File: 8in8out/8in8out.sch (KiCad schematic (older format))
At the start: 122 parts, among them IC1 ATTINY2313-P, J1 RJ45, J2 RJ45, J3 CONN_6, K110 G5T-1-12VDC, K120 G5T-1-12VDC, K130 G5T-1-12VDC, K140 G5T-1-12VDC, K150 G5T-1-12VDC, K160 G5T-1-12VDC, K170 G5T-1-12VDC, K180 G5T-1-12VDC, P1 CONN_5, P100 CONN_2, P101 CONN_2, P102 CONN_2, P103 CONN_2, P105 CONN_2, P106 CONN_2, P107 CONN_3, P109 CONN_2, P110 CONN_2, P120 CONN_2, P130 CONN_2, P140 CONN_2, P150 CONN_2, P160 CONN_2, P170 CONN_2, P180 CONN_2, P2 CONN_5, Q110 NPN, Q120 NPN, Q130 NPN, Q140 NPN, Q150 NPN, Q160 NPN, Q170 NPN, Q180 NPN, U1 74HC595, U10 OPTO-TRANSISTOR, U2 74LS165, U20 OPTO-TRANSISTOR, U30 OPTO-TRANSISTOR, U40 OPTO-TRANSISTOR, U50 OPTO-TRANSISTOR, U60 OPTO-TRANSISTOR, U70 OPTO-TRANSISTOR, U80 OPTO-TRANSISTOR

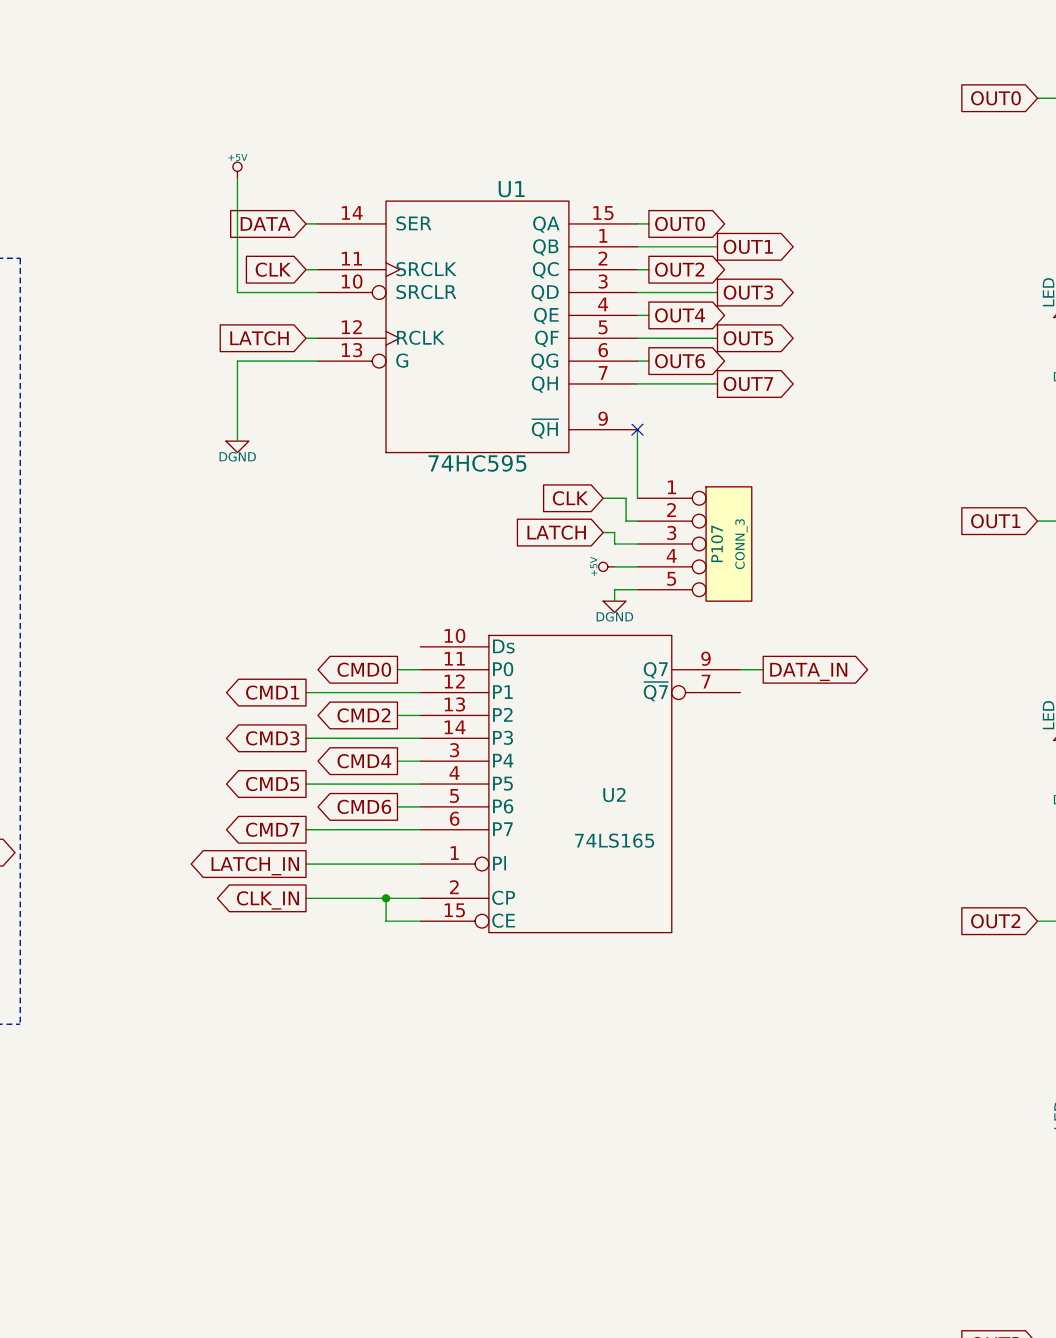
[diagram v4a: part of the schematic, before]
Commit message: Modification 74HC165
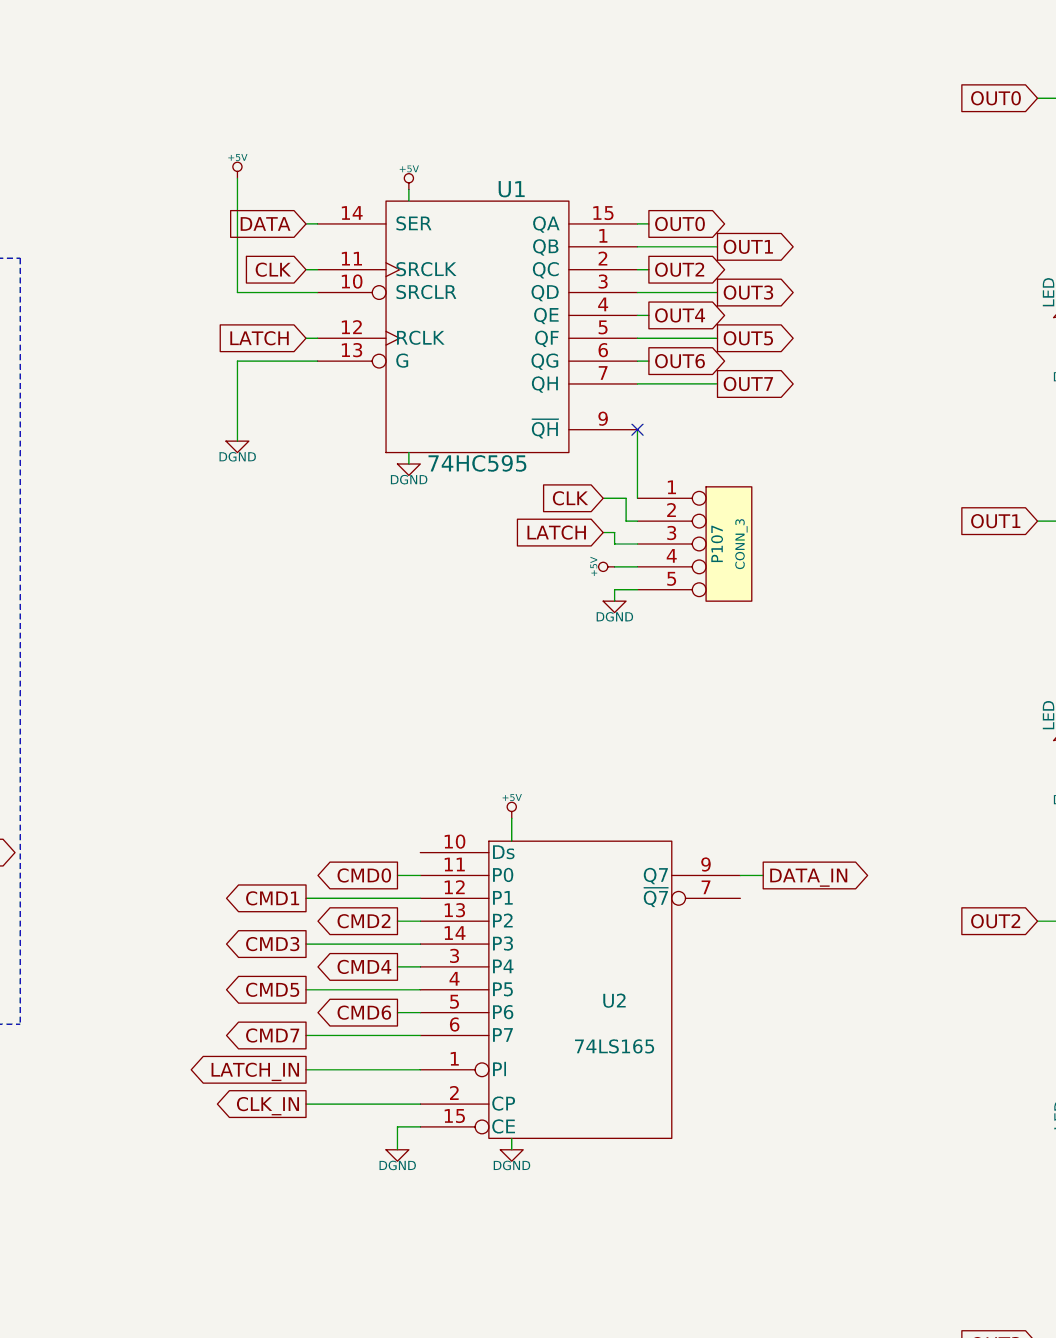
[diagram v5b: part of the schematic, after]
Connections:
- net GND is gone; now on net DGND: P1.5, P2.5, R10.2, R11.2, R20.2, R21.2, R30.2, R31.2, R40.2, R41.2, R50.2, R51.2, R60.2, R61.2, R70.2, R71.2, R80.2, R81.2, U1.8 (GND), U2.8 (GND)
- net CLK_IN: no longer U2.15 (CE)
- net DGND: now also U2.15 (CE)
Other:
- moved on the sheet: U2
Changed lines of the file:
@@
-EESchema Schematic File Version 2  date dim. 10 févr. 2013 15:59:09 CET
+EESchema Schematic File Version 2  date dim. 10 févr. 2013 20:44:48 CET
 LIBS:g5la-1-12vdc
 LIBS:power
@@
 Text GLabel 3950 13200 2    60   Input ~ 0
 CMD7
-Text GLabel 11200 8000 0    60   Output ~ 0
+Text GLabel 11200 8900 0    60   Output ~ 0
 CMD2
-Text GLabel 11200 7800 0    60   Output ~ 0
+Text GLabel 11200 8700 0    60   Output ~ 0
 CMD0
-Text GLabel 10800 8100 0    60   Output ~ 0
+Text GLabel 10800 9000 0    60   Output ~ 0
 CMD3
-Text GLabel 10800 7900 0    60   Output ~ 0
+Text GLabel 10800 8800 0    60   Output ~ 0
 CMD1
-Text GLabel 11200 8200 0    60   Output ~ 0
+Text GLabel 11200 9100 0    60   Output ~ 0
 CMD4
 Text GLabel 8850 7800 2    60   Output ~ 0
@@
 Wire Notes Line
 	5550 5800 5550 3500
-Text GLabel 10800 8500 0    60   Output ~ 0
+Text GLabel 10800 9400 0    60   Output ~ 0
 CMD7
-Text GLabel 11200 8400 0    60   Output ~ 0
+Text GLabel 11200 9300 0    60   Output ~ 0
 CMD6
-Text GLabel 10800 8300 0    60   Output ~ 0
+Text GLabel 10800 9200 0    60   Output ~ 0
 CMD5
 Wire Notes Line
@@
 L 74LS165 U2
 U 1 1 5116CE96
-P 12000 8300
-F 0 "U2" H 12150 8250 60  0000 C CNN
-F 1 "74LS165" H 12150 8050 60  0000 C CNN
-	1    12000 8300
+P 12000 9200
+F 0 "U2" H 12150 9150 60  0000 C CNN
+F 1 "74LS165" H 12150 8950 60  0000 C CNN
+	1    12000 9200
 	1    0    0    -1
 $EndComp
 Wire Wire Line
-	10800 7900 11300 7900
+	10800 8800 11300 8800
 Wire Wire Line
-	11300 8000 11200 8000
+	11300 8900 11200 8900
 Wire Wire Line
-	10800 8100 11300 8100
+	10800 9000 11300 9000
 Wire Wire Line
-	11300 8200 11200 8200
+	11300 9100 11200 9100
 Wire Wire Line
-	10800 8300 11300 8300
+	10800 9200 11300 9200
 Wire Wire Line
-	11300 8400 11200 8400
+	11300 9300 11200 9300
 Wire Wire Line
-	10800 8500 11300 8500
-Text GLabel 10800 8650 0    60   Output ~ 0
+	10800 9400 11300 9400
+Text GLabel 10800 9550 0    60   Output ~ 0
 LATCH_IN
-Text GLabel 10800 8800 0    60   Output ~ 0
+Text GLabel 10800 9700 0    60   Output ~ 0
 CLK_IN
 Wire Wire Line
-	11300 8650 10800 8650
+	11300 9550 10800 9550
 Text GLabel 9050 3100 3    60   Output ~ 0
 A0
@@
 	8350 8200 8400 8200
 Wire Wire Line
-	10800 8800 11300 8800
-Wire Wire Line
-	11150 8900 11300 8900
-Text GLabel 12800 7800 2    60   Output ~ 0
+	10800 9700 11300 9700
+Text GLabel 12800 8700 2    60   Output ~ 0
 DATA_IN
 Wire Wire Line
-	11150 8900 11150 8800
-Connection ~ 11150 8800
-Wire Wire Line
 	5950 7600 6050 7600
 Wire Wire Line
@@
 DATA_IN
 Wire Wire Line
-	11300 7800 11200 7800
+	11300 8700 11200 8700
 NoConn ~ 12250 6750
 Wire Wire Line
@@
 $EndComp
 $Comp
-L +5V #PWR093
+L +5V #PWR091
 U 1 1 51172614
 P 3800 2550
-F 0 "#PWR093" H 3800 2640 20  0001 C CNN
+F 0 "#PWR091" H 3800 2640 20  0001 C CNN
 F 1 "+5V" H 3800 2640 30  0000 C CNN
 	1    3800 2550
@@
 $EndComp
 $Comp
-L +5V #PWR094
+L +5V #PWR092
 U 1 1 51172694
 P 3800 4000
-F 0 "#PWR094" H 3800 4090 20  0001 C CNN
+F 0 "#PWR092" H 3800 4090 20  0001 C CNN
 F 1 "+5V" H 3800 4090 30  0000 C CNN
 	1    3800 4000
@@
 $EndComp
 $Comp
-L +5V #PWR095
+L +5V #PWR093
 U 1 1 511726A0
 P 3800 5450
-F 0 "#PWR095" H 3800 5540 20  0001 C CNN
+F 0 "#PWR093" H 3800 5540 20  0001 C CNN
 F 1 "+5V" H 3800 5540 30  0000 C CNN
 	1    3800 5450
@@
 $EndComp
 $Comp
-L +5V #PWR096
+L +5V #PWR094
 U 1 1 511726AC
 P 3800 6900
-F 0 "#PWR096" H 3800 6990 20  0001 C CNN
+F 0 "#PWR094" H 3800 6990 20  0001 C CNN
 F 1 "+5V" H 3800 6990 30  0000 C CNN
 	1    3800 6900
@@
 $EndComp
 $Comp
-L +5V #PWR097
+L +5V #PWR095
 U 1 1 511726B8
 P 3800 8350
-F 0 "#PWR097" H 3800 8440 20  0001 C CNN
+F 0 "#PWR095" H 3800 8440 20  0001 C CNN
 F 1 "+5V" H 3800 8440 30  0000 C CNN
 	1    3800 8350
@@
 $EndComp
 $Comp
-L +5V #PWR098
+L +5V #PWR096
 U 1 1 511726C4
 P 3800 9800
-F 0 "#PWR098" H 3800 9890 20  0001 C CNN
+F 0 "#PWR096" H 3800 9890 20  0001 C CNN
 F 1 "+5V" H 3800 9890 30  0000 C CNN
 	1    3800 9800
@@
 $EndComp
 $Comp
-L +5V #PWR099
+L +5V #PWR097
 U 1 1 511726D0
 P 3800 11250
-F 0 "#PWR099" H 3800 11340 20  0001 C CNN
+F 0 "#PWR097" H 3800 11340 20  0001 C CNN
 F 1 "+5V" H 3800 11340 30  0000 C CNN
 	1    3800 11250
@@
 $EndComp
 $Comp
-L +5V #PWR0100
+L +5V #PWR098
 U 1 1 511726DC
 P 3800 12700
-F 0 "#PWR0100" H 3800 12790 20  0001 C CNN
+F 0 "#PWR098" H 3800 12790 20  0001 C CNN
 F 1 "+5V" H 3800 12790 30  0000 C CNN
 	1    3800 12700
@@
 	5250 9350 5550 9350
 $Comp
-L GND #PWR?
+L GND #PWR099
 U 1 1 51176AB9
 P 6800 13300
-F 0 "#PWR?" H 6800 13300 30  0001 C CNN
+F 0 "#PWR099" H 6800 13300 30  0001 C CNN
 F 1 "GND" H 6800 13230 30  0001 C CNN
 	1    6800 13300
@@
 $EndComp
 $Comp
-L GND #PWR?
+L GND #PWR0100
 U 1 1 51176ACB
 P 6800 13950
-F 0 "#PWR?" H 6800 13950 30  0001 C CNN
+F 0 "#PWR0100" H 6800 13950 30  0001 C CNN
 F 1 "GND" H 6800 13880 30  0001 C CNN
 	1    6800 13950
@@
 $EndComp
 Wire Wire Line
-	12700 7800 12800 7800
+	12700 8700 12800 8700
 Wire Wire Line
 	12100 7050 12200 7050
@@
 	12150 7450 12150 7500
 $Comp
-L DGND #PWR?
+L DGND #PWR0101
 U 1 1 5117C4D5
 P 12150 7500
-F 0 "#PWR?" H 12150 7500 40  0001 C CNN
+F 0 "#PWR0101" H 12150 7500 40  0001 C CNN
 F 1 "DGND" H 12150 7430 40  0000 C CNN
 	1    12150 7500
@@
 $EndComp
 $Comp
-L +5V #PWR?
+L +5V #PWR0102
 U 1 1 5117C4DB
 P 12150 7350
-F 0 "#PWR?" H 12150 7440 20  0001 C CNN
+F 0 "#PWR0102" H 12150 7440 20  0001 C CNN
 F 1 "+5V" H 12150 7440 30  0000 C CNN
 	1    12150 7350
 	0    -1   -1   0
 $EndComp
+$Comp
+L DGND #PWR?
+U 1 1 5117C690
+P 11200 9900
+F 0 "#PWR?" H 11200 9900 40  0001 C CNN
+F 1 "DGND" H 11200 9830 40  0000 C CNN
+	1    11200 9900
+	1    0    0    -1
+$EndComp
+Wire Wire Line
+	11300 9800 11200 9800
+Wire Wire Line
+	11200 9800 11200 9900
+$Comp
+L +5V #PWR?
+U 1 1 5117FE90
+P 11700 8450
+F 0 "#PWR?" H 11700 8540 20  0001 C CNN
+F 1 "+5V" H 11700 8540 30  0000 C CNN
+	1    11700 8450
+	1    0    0    -1
+$EndComp
+$Comp
+L DGND #PWR?
+U 1 1 5117FE96
+P 11700 9900
+F 0 "#PWR?" H 11700 9900 40  0001 C CNN
+F 1 "DGND" H 11700 9830 40  0000 C CNN
+	1    11700 9900
+	1    0    0    -1
+$EndComp
+Wire Wire Line
+	11700 9850 11700 9900
+Wire Wire Line
+	11250 6850 11250 6900
+Wire Wire Line
+	11250 5750 11250 5700
+Wire Wire Line
+	11700 8450 11700 8550
+$Comp
+L +5V #PWR?
+U 1 1 51180484
+P 11250 5700
+F 0 "#PWR?" H 11250 5790 20  0001 C CNN
+F 1 "+5V" H 11250 5790 30  0000 C CNN
+	1    11250 5700
+	1    0    0    -1
+$EndComp
+$Comp
+L DGND #PWR?
+U 1 1 5118048A
+P 11250 6900
+F 0 "#PWR?" H 11250 6900 40  0001 C CNN
+F 1 "DGND" H 11250 6830 40  0000 C CNN
+	1    11250 6900
+	1    0    0    -1
+$EndComp
 $EndSCHEMATC

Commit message: Routage, diverses ameliorations
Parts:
- removed D10, D110, D120, D130, D140, D150, D160, D170, D180, D20, D30, D40, D50, D60, D70, D80: LED, symbol LED
- removed IC1: ATTINY2313-P, DIP20, symbol ATTINY2313-P
- removed P107: CONN_3, symbol CONN_5
- removed P109: CONN_2, symbol CONN_2
- removed R10, R110, R12, R120, R130, R140, R150, R160, R170, R180, R20, R22, R30, R32, R40, R42, R50, R52, R60, R62, R70, R72, R80, R82: R, symbol R
- removed U1: 74HC595, symbol 74HC595
- removed U2: 74LS165, symbol 74LS165
- added IC1: ATTINY48-A, TQFP32, symbol ATTINY48-A
- added P3: CONN_10X2, symbol CONN_10X2
- added P4: CONN_2, symbol CONN_2
- added U1: 78L05, symbol 78L05
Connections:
- net +12V: now also U1.VI
- net +5V: now also IC1.18 (AVCC), IC1.4 (VCC), P3.19 (P19), P4.2 (PM), U1.VO; no longer J1.7, J1.8, J2.7, J2.8, J3.1
- net /INT: now also IC1.31 ((PCINT17)PD1)
- net A0: now also IC1.1 ((PCINT19/INT1)PD3)
- net A1: now also IC1.2 ((PCINT20/T0)PD4)
- net A2: now also IC1.3 ((PCINT26)PA2)
- net A3: now also IC1.6 ((PCINT27)PA3)
- net CMD0: now also IC1.30 ((PCINT16)PD0), P3.1 (P1)
- net CMD1: now also IC1.26 ((PCINT11/ADC3)PC3), P3.3 (P3)
- net CMD2: now also IC1.25 ((PCINT10/ADC2)PC2), P3.5 (P5)
- net CMD3: now also IC1.24 ((PCINT9/ADC1)PC1), P3.7 (P7)
- net CMD4: now also IC1.23 ((PCINT8/ADC0)PC0), P3.9 (P9)
- net CMD5: now also IC1.22 ((PCINT25/ADC7)PA1), P3.11 (P11)
- net CMD6: now also IC1.20 ((PCINT15)PC7), P3.13 (P13)
- net CMD7: now also IC1.19 ((PCINT24/ADC6)PA0), P3.15 (P15)
- net MISO: now also IC1.16 ((PCINT4/MISO)PB4)
- net OUT0: now also IC1.14 ((PCINT2/OC1B/~SS~)PB2), P3.2 (P2)
- net OUT1: now also IC1.13 ((PCINT1/OC1A)PB1), P3.4 (P4)
- net OUT2: now also IC1.12 ((PCINT0/CLKO/ICP1)PB0), P3.6 (P6)
- net OUT3: now also IC1.11 ((PCINT23/AIN1)PD7), P3.8 (P8)
- net OUT4: now also IC1.10 ((PCINT22/AIN0)PD6), P3.10 (P10)
- net OUT5: now also IC1.9 ((PCINT21/T1)PD5), P3.12 (P12)
- net OUT6: now also IC1.8 ((PCINT7)PB7), P3.14 (P14)
- net OUT7: now also IC1.7 ((PCINT6/CLKI)PB6), P3.16 (P16)
- net RESET: now also R4.2, IC1.29 ((PCINT14/~RESET~)PC6), P3.17 (P17)
- net LED: now reaches D3.1 (A)
- net LED: now also IC1.32 ((PCINT18/INT0)PD2), P3.18 (P18)
- net DGND renamed GND
- net GND: now also IC1.21 (GND), IC1.5 (GND), P3.20 (P20), U1.GND; no longer P1.5, P2.5, R11.2, R21.2, R31.2, R41.2, R51.2, R61.2, R71.2, R81.2
- net MOSI(SDA) renamed SDA
- net SDA: now also IC1.27 ((PCINT12/SDA/ADC4)PC4); no longer ISP0.4
- net SCK(SCL) renamed SCL
- net SCL: now also IC1.28 ((PCINT13/SCL/ADC5)PC5); no longer ISP0.3
- new net 5V_EXT: J1.7, J1.8, J2.7, J2.8, J3.1, P4.1 (P1)
- new net COM0: P1.5, R11.2, R21.2, R31.2, R41.2
- new net COM1: P2.5, R51.2, R61.2, R71.2, R81.2
- new net MOSI: IC1.15 ((PCINT3/MOSI)PB3), ISP0.4
- new net SCK: IC1.17 ((PCINT5/SCK)PB5), ISP0.3
- no-connect marks 10 -> 9
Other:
- moved on the sheet: D151, D161, D3, ISP0, K150, K160, P150, P160, Q150, Q160, R11, R151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

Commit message: Remplacement des transistors et diodes de roues libres par un ULN2803
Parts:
- removed D111, D121, D131, D141, D151, D161, D171, D181: DIODE, symbol DIODE
- removed Q110, Q120, Q130, Q140, Q150, Q160, Q170, Q180: NPN, symbol NPN
- removed R111, R121, R131, R141, R151, R161, R171, R181: R, symbol R
- removed U1: 78L05, symbol 78L05
- added U1: 7805, symbol 7805
- added U2: ULN2803, symbol ULN2803
- R1, R3: value R -> 2KR
- R2: value R -> 4.7KR
- R4: value R -> 10KR
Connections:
- net +12V: now also U1.VI, U2.10 (COM)
- net +5V: now also P3.20 (P20), U1.VO; no longer P3.19 (P19)
- net GND: now also P3.19 (P19), U1.GND, U2.9 (GND); no longer P3.20 (P20)
- net OUT0: now also U2.1 (I1)
- net OUT1: now also U2.2 (I2)
- net OUT2: now also U2.3 (I3)
- net OUT3: now also U2.4 (I4)
- net OUT4: now also IC1.7 ((PCINT6/CLKI)PB6), U2.5 (I5); no longer IC1.10 ((PCINT22/AIN0)PD6)
- net OUT5: now also IC1.8 ((PCINT7)PB7), U2.6 (I6); no longer IC1.9 ((PCINT21/T1)PD5)
- net OUT6: now also IC1.9 ((PCINT21/T1)PD5), U2.7 (I7); no longer IC1.8 ((PCINT7)PB7)
- net OUT7: now also IC1.10 ((PCINT22/AIN0)PD6), U2.8 (I8); no longer IC1.7 ((PCINT6/CLKI)PB6)
- net R0: now reaches K110.2 (C2)
- net R0: now also U2.18 (O1)
- net R1: now reaches K120.2 (C2)
- net R1: now also U2.17 (O2)
- net R2: now reaches K130.2 (C2)
- net R2: now also U2.16 (O3)
- net R3: now reaches K140.2 (C2)
- net R3: now also U2.15 (O4)
- net R4: now reaches K150.2 (C2)
- net R4: now also U2.14 (O5)
- net R5: now reaches K160.2 (C2)
- net R5: now also U2.13 (O6)
- net R6: now reaches K170.2 (C2)
- net R6: now also U2.12 (O7)
- net R7: now reaches K180.2 (C2)
- net R7: now also U2.11 (O8)
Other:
- note added: "2x 4 INPUTS (9~12V)"
- note added: "EXTERNAL CONNECTOR (extension)"
- note added: "RELAYS COMMAND"
- note added: "built-in +5V"
- note added: "or external +5V"
- moved on the sheet: C1, C2, D1, D2, D3, IC1, ISP0, J1, J2, J3, K150, K160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
